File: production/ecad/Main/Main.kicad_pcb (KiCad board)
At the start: 4 copper layers, 51.5 x 76.5 mm, 50 parts, among them J1 214721-0061, J10 214721-0061, J11 2147210040, J2 214721-0100, J3 214721-0080, J4 214721-0020, J5 214721-0020, J6 214721-0020, J7 ADC-028-1-T/R-PA10T, J8 61301611821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

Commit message: more changes
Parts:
- added G***: LOGO, LOGO, F.Cu at (121.5, 124.5)
- added G***: LOGO, LOGO, F.Cu at (77.5, 139.5)
- added G***: LOGO, LOGO, F.Cu at (78.5, 150.5)
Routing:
- net GND: vias 40 -> 49

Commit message: silkscreen artwork
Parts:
- removed the G*** at (121.5, 124.5)
- removed the G*** at (77.5, 139.5)
- removed the G*** at (78.5, 150.5)
- added G***: LOGO, LOGO, F.Cu at (63.5, 112.5)
- added G***: LOGO, LOGO, F.Cu at (62.0, 125.0)
- added G***: LOGO, LOGO, F.Cu at (67.5, 69.5)
- added G***: LOGO, LOGO, F.Cu at (62.5, 86.5)
- added G***: LOGO, LOGO, F.Cu at (79.5, 76.0)

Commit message: final changes
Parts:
- moved Q2 2.32 mm to (89.5, 124.0)
- moved Q3 2.05 mm to (91.1, 58.0)
- moved R7 0.67 mm to (94.0, 62.7)
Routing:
- net 5VEXT: track 147.6 -> 142.8 mm, vias 18 -> 16
- net 3V3EXT: track 168.6 -> 165.9 mm
- net Net-(Q2-S): track 11.6 -> 9.70 mm
- net VBR_MTR_EN1: track 40.8 -> 42.4 mm
- net Net-(Q3-B): track 11.0 -> 10.2 mm
- net Net-(U3-RATE): track 15.2 -> 14.6 mm
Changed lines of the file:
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@@
 	(footprint "LoadCellFootprints:mmbt4403"
 		(layer "F.Cu")
-		(at 92.5 59.5 90)
+		(at 91.1 58 90)
 		(descr "<b>TO-236</b> ITT Intermetall")
 		(property "Reference" "Q3"
@@
 		(at 87 61)
 		(property "Reference" "DNP3"
-			(at 0.025 -0.4 0)
+			(at 0 -1 0)
 			(layer "F.SilkS")
 			(effects
 				(font
-					(size 0.64 0.64)
-					(thickness 0.15)
+					(size 0.5 0.5)
+					(thickness 0.05)
 				)
 			)
@@
 	(footprint "Transistor_Power:GaN_Systems_GaNPX-3_5x6.6mm_Drain3.76x0.6mm"
 		(layer "F.Cu")
-		(at 91.73 124.63 180)
+		(at 89.5 124 180)
 		(descr "GaN Systems GaNPX GS66504B Package, https://gansystems.com/wp-content/uploads/2020/04/GS66504B-DS-Rev-200402.pdf")
 		(tags "ganpx gs66504b")
@@
 	(footprint "LoadCellFootprints:10k"
 		(layer "F.Cu")
-		(at 94.67 62.675 180)
+		(at 94 62.675 180)
 		(property "Reference" "R7"
 			(at -1.83 -0.825 180)
@@
 	)
 	(segment
+		(start 85.5 127)
+		(end 89.41 127)
+		(width 0.2)
+		(layer "F.Cu")
+		(net 1)
+	)
+	(segment
 		(start 91 101)
 		(end 93.0875 101)
@@
 	)
 	(segment
-		(start 91.73 127.54)
-		(end 88.73 127.54)
+		(start 80.73 121.04)
+		(end 85.5 121.04)
 		(width 0.2)
 		(layer "F.Cu")
@@
 	)
 	(segment
+		(start 89.41 127)
+		(end 89.5 126.91)
+		(width 0.2)
+		(layer "F.Cu")
+		(net 1)
+	)
+	(segment
 		(start 69.83 81.54)
 		(end 69.93 81.44)
@@
 		(net 1)
 	)
-	(segment
-		(start 80.73 121.04)
-		(end 88.73 121.04)
-		(width 0.2)
-		(layer "F.Cu")
-		(net 1)
-	)
 	(via
 		(at 71.13 76.84)
@@
 	)
 	(via
-		(at 88.73 127.54)
+		(at 85.5 127)
 		(size 0.6)
 		(drill 0.3)
@@
 	)
 	(via
-		(at 88.73 121.04)
+		(at 85.5 121.04)
 		(size 0.6)
 		(drill 0.3)
@@
 	)
 	(segment
-		(start 88.73 127.54)
-		(end 88.73 121.04)
-		(width 0.2)
-		(layer "B.Cu")
-		(net 1)
-	)
-	(segment
 		(start 80.73 119.04)
 		(end 80.73 121.04)
@@
 	)
 	(segment
+		(start 85.5 127)
+		(end 85.5 121.04)
+		(width 0.2)
+		(layer "B.Cu")
+		(net 1)
+	)
+	(segment
 		(start 75.23 77.94)
 		(end 75.23 91.54)
@@
 	)
 	(via
-		(at 92.25 63)
+		(at 98.5 63.5)
 		(size 0.6)
 		(drill 0.3)
@@
 	)
 	(segment
+		(start 93.22 64.605)
+		(end 93.22 62.675)
+		(width 0.2)
+		(layer "F.Cu")
+		(net 3)
+	)
+	(segment
 		(start 92.18 108.54)
 		(end 92.23 108.49)
@@
 	)
 	(segment
+		(start 89 59)
+		(end 89 57.2)
+		(width 0.2)
+		(layer "F.Cu")
+		(net 3)
+	)
+	(segment
 		(start 80.73 116.54)
 		(end 90.73 116.54)
@@
 	)
 	(segment
-		(start 90.78 111.09)
-		(end 90.73 111.04)
+		(start 89.15 57.05)
+		(end 92.2 57.05)
 		(width 0.2)
 		(layer "F.Cu")
@@
 	)
 	(segment
-		(start 93.6 58.55)
-		(end 94.95 58.55)
-		(width 0.2)
-		(layer "F.Cu")
-		(net 3)
-	)
-	(segment
-		(start 94.95 58.55)
-		(end 95 58.5)
+		(start 90.78 111.09)
+		(end 90.73 111.04)
 		(width 0.2)
 		(layer "F.Cu")
@@
 	)
 	(segment
+		(start 89 57.2)
+		(end 89.15 57.05)
+		(width 0.2)
+		(layer "F.Cu")
+		(net 3)
+	)
+	(segment
 		(start 77.605 116.56)
 		(end 77.28 116.885)
@@
 	)
 	(segment
-		(start 93.89 62.675)
-		(end 93.89 64.835)
-		(width 0.2)
-		(layer "F.Cu")
-		(net 3)
-	)
-	(segment
 		(start 69.79 120.1)
 		(end 71.73 120.1)
@@
 	)
 	(segment
-		(start 90.318626 58.55)
-		(end 89.434313 59.434313)
-		(width 0.2)
-		(layer "F.Cu")
-		(net 3)
-	)
-	(segment
 		(start 84.5 62.5)
 		(end 87.957 62.5)
@@
 	)
 	(segment
-		(start 95 61.565)
-		(end 93.89 62.675)
-		(width 0.2)
-		(layer "F.Cu")
-		(net 3)
-	)
-	(segment
-		(start 95 61.5)
-		(end 95 61.565)
-		(width 0.2)
-		(layer "F.Cu")
-		(net 3)
-	)
-	(segment
-		(start 93.89 64.835)
-		(end 93.67 65.055)
-		(width 0.2)
-		(layer "F.Cu")
-		(net 3)
-	)
-	(segment
 		(start 57.2 105)
 		(end 56.5 105)
@@
 	)
 	(segment
-		(start 93.6 58.55)
-		(end 90.318626 58.55)
-		(width 0.2)
-		(layer "F.Cu")
-		(net 3)
-	)
-	(segment
 		(start 76.32 61)
 		(end 84.5 61)
@@
 	)
 	(segment
+		(start 93.67 65.055)
+		(end 93.22 64.605)
+		(width 0.2)
+		(layer "F.Cu")
+		(net 3)
+	)
+	(segment
 		(start 89.4 63)
 		(end 88.407 63)
@@
 		(net 3)
 	)
+	(segment
+		(start 89.434313 59.434313)
+		(end 89 59)
+		(width 0.2)
+		(layer "F.Cu")
+		(net 3)
+	)
 	(via
 		(at 95.5 66.995)
@@
 	)
 	(via
-		(at 95 58.5)
-		(size 0.6)
-		(drill 0.3)
-		(layers "F.Cu" "B.Cu")
-		(net 3)
-	)
-	(via
 		(at 57.2 94.005863)
 		(size 0.6)
@@
 	)
 	(via
-		(at 95 61.5)
-		(size 0.6)
-		(drill 0.3)
-		(layers "F.Cu" "B.Cu")
-		(net 3)
-	)
-	(via
 		(at 80.73 95.54)
 		(size 0.6)
@@
 	)
 	(segment
-		(start 95 58.5)
-		(end 95 61.5)
-		(width 0.2)
-		(layer "B.Cu")
-		(net 3)
-	)
-	(segment
 		(start 75.5 60.1)
 		(end 75.5 60.82)
@@
 	)
 	(segment
-		(start 95 63.125)
-		(end 95.45 62.675)
-		(width 0.2)
-		(layer "F.Cu")
-		(net 6)
-	)
-	(segment
 		(start 87.78 61)
 		(end 90.1 61)
@@
 	)
 	(segment
-		(start 93.86 122.82)
-		(end 94.45 122.82)
+		(start 95.23 115.04)
+		(end 95.39 115.2)
 		(width 0.2)
 		(layer "F.Cu")
@@
 	)
 	(segment
-		(start 95.23 115.04)
-		(end 95.39 115.2)
+		(start 91.63 122.19)
+		(end 94.54 122.19)
 		(width 0.2)
 		(layer "F.Cu")
@@
 	)
 	(segment
-		(start 94.45 122.82)
-		(end 94.73 122.54)
+		(start 94.54 122.19)
+		(end 94.73 122)
 		(width 0.2)
 		(layer "F.Cu")
@@
 	)
 	(via
-		(at 94.73 122.54)
+		(at 94.73 122)
 		(size 0.6)
 		(drill 0.3)
@@
 	)
 	(segment
-		(start 95.03 115.24)
-		(end 95.23 115.04)
+		(start 94.73 122)
+		(end 94.73 118.04)
 		(width 0.2)
 		(layer "B.Cu")
@@
 	)
 	(segment
-		(start 95.03 117.74)
-		(end 95.03 115.24)
+		(start 95.03 115.24)
+		(end 95.23 115.04)
 		(width 0.2)
 		(layer "B.Cu")
@@
 	)
 	(segment
-		(start 94.73 122.54)
-		(end 94.73 118.04)
+		(start 95.03 117.74)
+		(end 95.03 115.24)
 		(width 0.2)
 		(layer "B.Cu")
@@
 	)
 	(segment
-		(start 91.18 122.96)
-		(end 79.75 122.96)
+		(start 79.63 122.84)
+		(end 88.44 122.84)
+		(width 0.2)
+		(layer "F.Cu")
+		(net 26)
+	)
+	(segment
+		(start 88.44 122.84)
+		(end 88.95 122.33)
 		(width 0.2)
 		(layer "F.Cu")
@@
 	)
 	(segment
+		(start 90.034313 59.965687)
+		(end 90.034313 58.034313)
+		(width 0.2)
+		(layer "F.Cu")
+		(net 42)
+	)
+	(segment
 		(start 88.425 67.5)
 		(end 88.33 67.595)
@@
 	)
 	(segment
-		(start 82.17 68.41)
-		(end 84.115 68.41)
+		(start 90.034313 58.034313)
+		(end 90 58)
 		(width 0.2)
 		(layer "F.Cu")
@@
 	)
 	(segment
-		(start 91.4 59.5)
-		(end 90.5 59.5)
+		(start 90 60)
+		(end 90.034313 59.965687)
 		(width 0.2)
 		(layer "F.Cu")
@@
 	)
 	(segment
-		(start 90.5 59.5)
-		(end 90 60)
+		(start 82.17 68.41)
+		(end 84.115 68.41)
 		(width 0.2)
 		(layer "F.Cu")
@@
 	)
 	(segment
-		(start 93.6 60.45)
-		(end 90.715687 60.45)
+		(start 90.6 60.565687)
+		(end 92.2 58.965687)
 		(width 0.2)
 		(layer "F.Cu")
@@
 	)
 	(segment
-		(start 90.715687 60.45)
-		(end 90.6 60.565687)
+		(start 92.2 58.965687)
+		(end 92.2 58.95)
 		(width 0.2)
 		(layer "F.Cu")

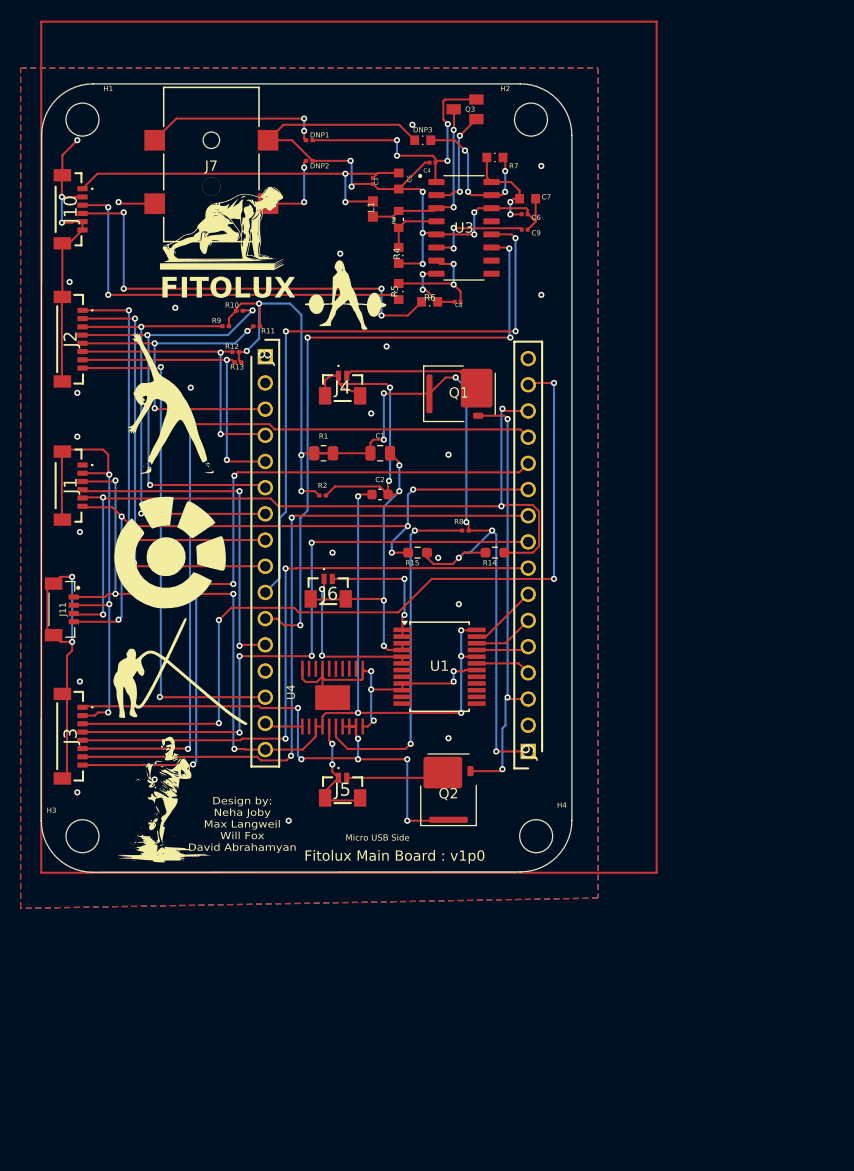
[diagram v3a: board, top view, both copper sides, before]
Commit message: resistor and inductor
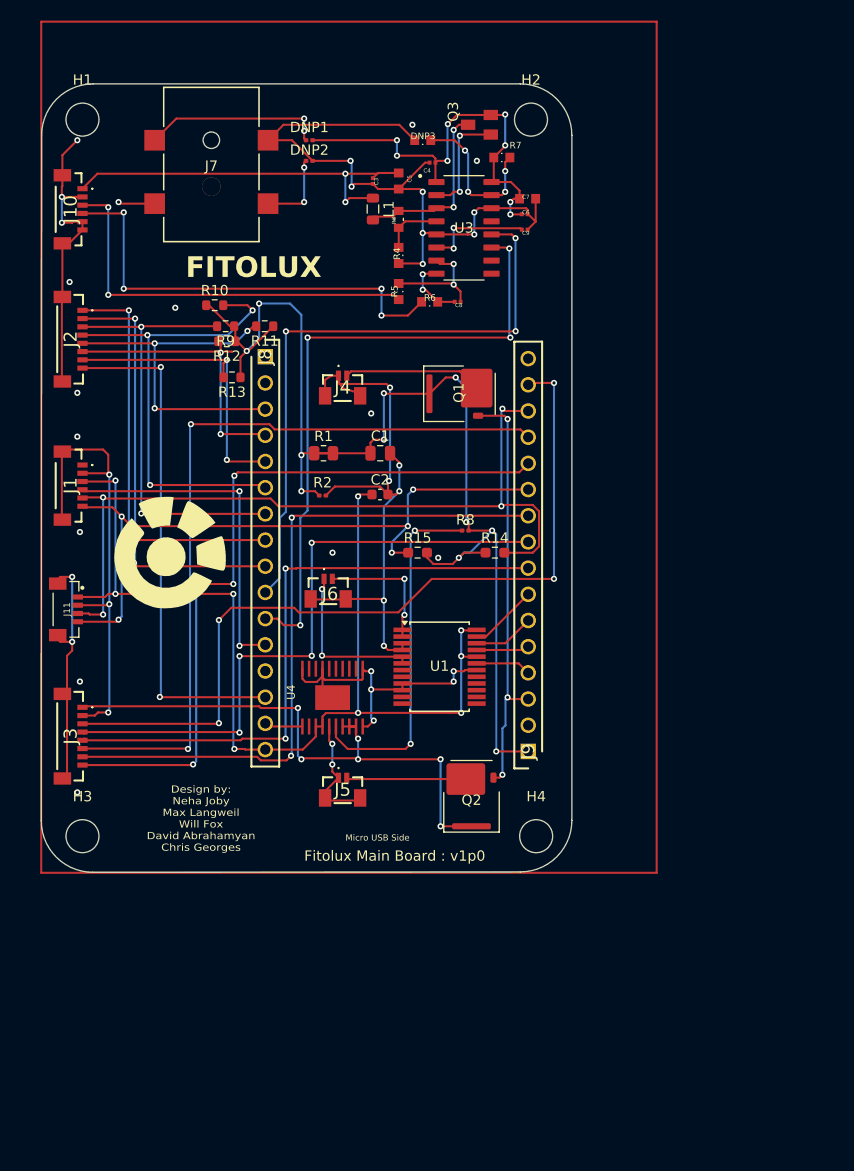
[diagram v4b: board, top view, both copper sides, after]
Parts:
- removed G*** (x5): LOGO, LOGO
- L1: footprint LoadCellFootprints:inductor -> Inductor_SMD:L_0805_2012Metric
- R10, R11, R12, R13, R9: footprint Resistor_SMD:R_0201_0603Metric -> Resistor_SMD:R_0603_1608Metric
- moved R10 2.46 mm to (66.8, 77.0)
- moved Q2 2.32 mm to (91.7, 124.6)
- moved Q3 2.05 mm to (92.5, 59.5)
- moved R13 1.57 mm to (68.5, 84.0)
- moved R12 1.34 mm to (68.0, 80.5)
- moved R11 0.79 mm to (71.7, 79.0)
- moved R7 0.67 mm to (94.7, 62.7)
- moved J11 0.40 mm to (52.4, 106.5)
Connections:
- Q2 pad 2: VBR_MTR_EN1 -> /Motor/VBR_MTR_EN2
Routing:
- net 3V3EXT: track 165.9 -> 173.1 mm
- net 5VEXT: track 142.8 -> 147.6 mm, vias 16 -> 18
- net ANO_SW2: track 44.4 -> 46.5 mm
- net Net-(Q2-S): track 9.70 -> 11.6 mm
- net VBR_MTR_EN1: track 42.4 -> 40.8 mm
- net ANO_SW4: track 26.8 -> 28.0 mm
- net ANO_SW5: track 28.4 -> 29.3 mm
- net Net-(Q3-B): track 10.2 -> 11.0 mm
- net Net-(U3-RATE): track 14.6 -> 15.2 mm
- net ANO_SW1: track 44.4 -> 43.9 mm
- net GND: vias 49 -> 40
- removed copper zone on B.Cu, net GND
- removed copper zone on F.Cu, net GND
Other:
- board text added: "Design by: Neha Joby Max Langweil Will Fox David Abrahamyan Chris Georges"
- board text removed: "Design by: Neha Joby Max Langweil Will Fox David Abrahamyan"

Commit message: footprints
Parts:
- DNP1, DNP2, R2, R8: footprint Resistor_SMD:R_0201_0603Metric -> Resistor_SMD:R_0603_1608Metric
- R1: footprint Resistor_SMD:R_0805_2012Metric -> Resistor_SMD:R_0603_1608Metric
- moved DNP2 0.50 mm to (76.0, 62.5)
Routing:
- net 3V3EXT: track 173.1 -> 170.5 mm
- net Net-(DNP2-Pad1): track 7.64 -> 8.20 mm
- net Net-(U4-RESET'_OR_PG): track 34.4 -> 33.9 mm
- net 5VEXT: track 147.6 -> 147.1 mm

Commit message: pcb
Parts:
- turned DNP2 to 180 degrees
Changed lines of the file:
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@@
 	(footprint "Resistor_SMD:R_0603_1608Metric"
 		(layer "F.Cu")
-		(at 76 62.5)
+		(at 76 62.5 180)
 		(descr "Resistor SMD 0603 (1608 Metric), square (rectangular) end terminal, IPC_7351 nominal, (Body size source: IPC-SM-782 page 72, https://www.pcb-3d.com/wordpress/wp-content/uploads/ipc-sm-782a_amendment_1_and_2.pdf), generated with kicad-footprint-generator")
 		(tags "resistor")
 		(property "Reference" "DNP2"
-			(at 0 -1.43 0)
+			(at 0 -1.43 360)
 			(layer "F.SilkS")
 			(effects
@@
 		)
 		(property "Value" "0"
-			(at 0 1.43 0)
+			(at 0 1.43 360)
 			(layer "F.Fab")
 			(effects
@@
 		)
 		(property "Footprint" "Resistor_SMD:R_0603_1608Metric"
-			(at 0 0 0)
+			(at 0 0 180)
 			(unlocked yes)
 			(layer "F.Fab")
@@
 		)
 		(property "Datasheet" ""
-			(at 0 0 0)
+			(at 0 0 180)
 			(unlocked yes)
 			(layer "F.Fab")
@@
 		)
 		(property "Description" "Resistor"
-			(at 0 0 0)
+			(at 0 0 180)
 			(unlocked yes)
 			(layer "F.Fab")
@@
 		(attr smd)
 		(fp_line
-			(start -0.237258 -0.5225)
-			(end 0.237258 -0.5225)
+			(start -0.237258 0.5225)
+			(end 0.237258 0.5225)
 			(stroke
 				(width 0.12)
@@
 		)
 		(fp_line
-			(start -0.237258 0.5225)
-			(end 0.237258 0.5225)
+			(start -0.237258 -0.5225)
+			(end 0.237258 -0.5225)
 			(stroke
 				(width 0.12)
@@
 		)
 		(fp_line
-			(start -1.48 -0.73)
-			(end 1.48 -0.73)
+			(start 1.48 0.73)
+			(end -1.48 0.73)
 			(stroke
 				(width 0.05)
@@
 		)
 		(fp_line
-			(start -1.48 0.73)
-			(end -1.48 -0.73)
+			(start 1.48 -0.73)
+			(end 1.48 0.73)
 			(stroke
 				(width 0.05)
@@
 		)
 		(fp_line
-			(start 1.48 -0.73)
-			(end 1.48 0.73)
+			(start -1.48 0.73)
+			(end -1.48 -0.73)
 			(stroke
 				(width 0.05)
@@
 		)
 		(fp_line
-			(start 1.48 0.73)
-			(end -1.48 0.73)
+			(start -1.48 -0.73)
+			(end 1.48 -0.73)
 			(stroke
 				(width 0.05)
@@
 		)
 		(fp_line
-			(start -0.8 -0.4125)
-			(end 0.8 -0.4125)
+			(start 0.8 0.4125)
+			(end -0.8 0.4125)
 			(stroke
 				(width 0.1)
@@
 		)
 		(fp_line
-			(start -0.8 0.4125)
-			(end -0.8 -0.4125)
+			(start 0.8 -0.4125)
+			(end 0.8 0.4125)
 			(stroke
 				(width 0.1)
@@
 		)
 		(fp_line
-			(start 0.8 -0.4125)
-			(end 0.8 0.4125)
+			(start -0.8 0.4125)
+			(end -0.8 -0.4125)
 			(stroke
 				(width 0.1)
@@
 		)
 		(fp_line
-			(start 0.8 0.4125)
-			(end -0.8 0.4125)
+			(start -0.8 -0.4125)
+			(end 0.8 -0.4125)
 			(stroke
 				(width 0.1)
@@
 		)
 		(fp_text user "${REFERENCE}"
-			(at 0 0 0)
+			(at 0 0 360)
 			(layer "F.Fab")
 			(effects
@@
 		)
 		(pad "1" smd roundrect
-			(at -0.825 0)
+			(at -0.825 0 180)
 			(size 0.8 0.95)
 			(layers "F.Cu" "F.Paste" "F.Mask")
@@
 		)
 		(pad "2" smd roundrect
-			(at 0.825 0)
+			(at 0.825 0 180)
 			(size 0.8 0.95)
 			(layers "F.Cu" "F.Paste" "F.Mask")
@@
 	)
 	(segment
-		(start 76.1 59.851471)
-		(end 76.1 61.775)
+		(start 56.465687 93.3)
+		(end 56.6 93.434313)
 		(width 0.2)
 		(layer "F.Cu")
@@
 	)
 	(segment
-		(start 75.748529 59.5)
-		(end 76.1 59.851471)
+		(start 52 65.5)
+		(end 52.05 65.45)
 		(width 0.2)
 		(layer "F.Cu")
@@
 	)
 	(segment
-		(start 56.465687 93.3)
-		(end 56.6 93.434313)
+		(start 83.63 95.36)
+		(end 84.41 95.36)
 		(width 0.2)
 		(layer "F.Cu")
@@
 	)
 	(segment
-		(start 52 65.5)
-		(end 52.05 65.45)
+		(start 84.73 92.54)
+		(end 84.73 92.26)
 		(width 0.2)
 		(layer "F.Cu")
@@
 	)
 	(segment
-		(start 83.63 95.36)
-		(end 84.41 95.36)
+		(start 75.175 62.5)
+		(end 73.5 62.5)
 		(width 0.2)
 		(layer "F.Cu")
@@
 	)
 	(segment
-		(start 84.73 92.54)
-		(end 84.73 92.26)
+		(start 73.5 62.5)
+		(end 72 61)
 		(width 0.2)
 		(layer "F.Cu")
@@
 	)
 	(segment
-		(start 76.1 61.775)
-		(end 76.825 62.5)
-		(width 0.2)
-		(layer "F.Cu")
-		(net 2)
-	)
-	(segment
 		(start 53.15 106.1)
 		(end 56.5 106.1)
@@
 	)
 	(segment
-		(start 75.175 63.3233)
-		(end 75.5 63.6483)
+		(start 75.6767 63.6483)
+		(end 76.542157 62.782843)
 		(width 0.2)
 		(layer "F.Cu")
@@
 	)
 	(segment
-		(start 75.175 62.5)
-		(end 75.175 63.3233)
+		(start 72 67.150001)
+		(end 75.349999 67.150001)
 		(width 0.2)
 		(layer "F.Cu")
@@
 	)
 	(segment
-		(start 72 67.150001)
-		(end 75.349999 67.150001)
+		(start 75.5 63.6483)
+		(end 75.6767 63.6483)
 		(width 0.2)
 		(layer "F.Cu")

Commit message: footprint
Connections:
- Q2 pad 2: /Motor/VBR_MTR_EN2 -> VBR_MTR_EN1
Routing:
- net VBR_MTR_EN1: track 40.8 -> 43.0 mm
- net GND: track 223.2 -> 221.3 mm
- net ANO_SW4: track 28.0 -> 27.1 mm
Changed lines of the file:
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@@
 	(net 69 "unconnected-(U4-NC3-PadP$13)")
 	(net 70 "/Load_Cell_and_Amplifier/AVDD")
-	(net 71 "/Motor/VBR_MTR_EN2")
 	(footprint "LOGO"
 		(layer "F.Cu")
@@
 			(layers "F.Cu" "F.Paste" "F.Mask")
 			(roundrect_rratio 0.25)
-			(net 71 "/Motor/VBR_MTR_EN2")
+			(net 23 "VBR_MTR_EN1")
 			(pinfunction "G")
 			(pintype "input")
@@
 	)
 	(segment
-		(start 75.251471 59.5)
-		(end 75.748529 59.5)
+		(start 77.28 114.085)
+		(end 78.255 115.06)
 		(width 0.2)
 		(layer "F.Cu")
@@
 	)
 	(segment
-		(start 77.28 114.085)
-		(end 78.255 115.06)
+		(start 78.11 95.46)
+		(end 78.985 94.585)
 		(width 0.2)
 		(layer "F.Cu")
@@
 	)
 	(segment
-		(start 78.11 95.46)
-		(end 78.985 94.585)
+		(start 52.05 64.4)
+		(end 52.05 62.55)
 		(width 0.2)
 		(layer "F.Cu")
@@
 	)
 	(segment
+		(start 52.05 62.55)
+		(end 51.5 62)
+		(width 0.2)
+		(layer "F.Cu")
+		(net 2)
+	)
+	(segment
 		(start 75.635 113.54)
 		(end 76.73 113.54)
@@
 	)
 	(segment
-		(start 52.05 62.45)
-		(end 53.5 61)
+		(start 51.5 62)
+		(end 51.55 62)
 		(width 0.2)
 		(layer "F.Cu")
@@
 	)
 	(segment
-		(start 52.05 64.4)
-		(end 52.05 62.45)
-		(width 0.2)
-		(layer "F.Cu")
-		(net 2)
-	)
-	(segment
 		(start 78.93 84.64)
 		(end 78.83 84.54)
@@
 	)
 	(via
-		(at 53.5 61)
+		(at 51.5 62)
 		(size 0.6)
 		(drill 0.3)
@@
 	)
 	(segment
+		(start 94.82 122.82)
+		(end 95.5 123.5)
+		(width 0.2)
+		(layer "F.Cu")
+		(net 23)
+	)
+	(segment
 		(start 92.37 87.72)
 		(end 94.91 87.72)
@@
 	)
 	(segment
-		(start 93.86 122.82)
-		(end 94.45 122.82)
-		(width 0.2)
-		(layer "F.Cu")
-		(net 23)
-	)
-	(segment
 		(start 95.23 115.04)
 		(end 95.39 115.2)
@@
 	)
 	(segment
-		(start 94.45 122.82)
-		(end 94.73 122.54)
+		(start 93.86 122.82)
+		(end 94.82 122.82)
 		(width 0.2)
 		(layer "F.Cu")
@@
 	)
 	(via
-		(at 94.73 122.54)
+		(at 95.5 123.5)
 		(size 0.6)
 		(drill 0.3)
@@
 	)
 	(segment
+		(start 95 122.81)
+		(end 94.73 122.54)
+		(width 0.2)
+		(layer "B.Cu")
+		(net 23)
+	)
+	(segment
 		(start 95.03 115.24)
 		(end 95.23 115.04)
@@
 	)
 	(segment
+		(start 95.5 123.5)
+		(end 95 123)
+		(width 0.2)
+		(layer "B.Cu")
+		(net 23)
+	)
+	(segment
+		(start 95 123)
+		(end 95 122.81)
+		(width 0.2)
+		(layer "B.Cu")
+		(net 23)
+	)
+	(segment
 		(start 95.03 117.74)
 		(end 95.03 115.24)
@@
 	(segment
 		(start 54 81.5)
-		(end 68.49 81.5)
+		(end 66.175 81.5)
 		(width 0.2)
 		(layer "F.Cu")
@@
 	)
 	(segment
-		(start 71.61 89.5)
-		(end 71.73 89.62)
+		(start 66.175 81.5)
+		(end 67.175 80.5)
 		(width 0.2)
 		(layer "F.Cu")
@@
 	)
 	(segment
-		(start 68.49 81.5)
-		(end 68.53 81.54)
+		(start 71.61 89.5)
+		(end 71.73 89.62)
 		(width 0.2)
 		(layer "F.Cu")

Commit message: error
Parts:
- moved R14 0.50 mm to (93.5, 101.0)
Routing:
- net GND: track 221.3 -> 220.7 mm
- net 3V3EXT: track 170.5 -> 169.9 mm
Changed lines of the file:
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@@
 	(footprint "Resistor_SMD:R_0603_1608Metric_Pad0.98x0.95mm_HandSolder"
 		(layer "F.Cu")
-		(at 94 101)
+		(at 93.5 101)
 		(descr "Resistor SMD 0603 (1608 Metric), square (rectangular) end terminal, IPC_7351 nominal with elongated pad for handsoldering. (Body size source: IPC-SM-782 page 72, https://www.pcb-3d.com/wordpress/wp-content/uploads/ipc-sm-782a_amendment_1_and_2.pdf), generated with kicad-footprint-generator")
 		(tags "resistor handsolder")
@@
 	)
 	(segment
-		(start 93.0875 101)
-		(end 92.9875 100.9)
-		(width 0.2)
-		(layer "F.Cu")
-		(net 1)
-	)
-	(segment
 		(start 76.4675 91.36)
 		(end 81.93 91.36)
@@
 	)
 	(segment
-		(start 91 101)
-		(end 93.0875 101)
-		(width 0.2)
-		(layer "F.Cu")
-		(net 1)
-	)
-	(segment
 		(start 91.73 127.54)
 		(end 88.73 127.54)
@@
 		(net 1)
 	)
+	(segment
+		(start 91 101)
+		(end 92.5875 101)
+		(width 0.2)
+		(layer "F.Cu")
+		(net 1)
+	)
 	(via
 		(at 71.13 76.84)
@@
 	)
 	(segment
-		(start 54 66.5)
-		(end 52 66.5)
-		(width 0.2)
-		(layer "F.Cu")
-		(net 2)
-	)
-	(segment
 		(start 97.95 68.895)
 		(end 97.17 69.675)
@@
 	)
 	(segment
+		(start 52 66.5)
+		(end 54 66.5)
+		(width 0.2)
+		(layer "F.Cu")
+		(net 2)
+	)
+	(segment
 		(start 77.28 112.99)
 		(end 77.28 112.26)
@@
 		(width 0.2)
 		(layer "F.Cu")
-		(net 2)
-	)
-	(segment
-		(start 53.35 66.5)
-		(end 54 66.5)
-		(width 0.2)
-		(layer "F.Cu")
